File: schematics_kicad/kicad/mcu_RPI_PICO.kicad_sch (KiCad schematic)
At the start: 0 parts

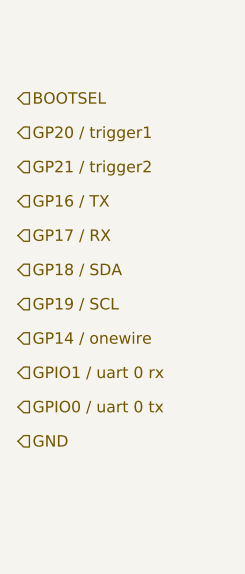
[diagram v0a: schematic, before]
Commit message: Updating schematics for RPI_PICO_W for tentacle v0.4
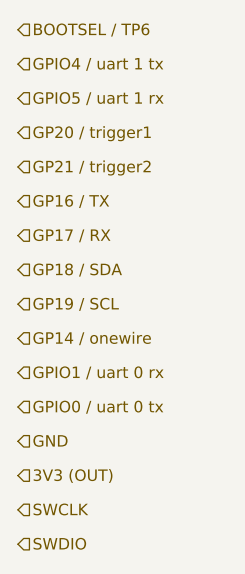
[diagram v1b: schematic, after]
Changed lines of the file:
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@@
 		(shape input)
 		(at 82.55 91.44 0)
-		(fields_autoplaced yes)
 		(effects
 			(font
@@
 		(shape input)
 		(at 82.55 99.06 0)
-		(fields_autoplaced yes)
 		(effects
 			(font
@@
 		(shape input)
 		(at 82.55 64.77 0)
-		(fields_autoplaced yes)
 		(effects
 			(font
@@
 		(shape input)
 		(at 82.55 83.82 0)
-		(fields_autoplaced yes)
 		(effects
 			(font
@@
 		(shape input)
 		(at 82.55 95.25 0)
-		(fields_autoplaced yes)
 		(effects
 			(font
@@
 		(shape input)
 		(at 82.55 87.63 0)
-		(fields_autoplaced yes)
+		(effects
+			(font
+				(size 1.27 1.27)
+			)
+			(justify left)
+		)
+	)
+	(hierarchical_label "GPIO4 {slash} uart 1 tx"
+		(shape input)
+		(at 82.55 57.15 0)
+		(effects
+			(font
+				(size 1.27 1.27)
+			)
+			(justify left)
+		)
+	)
+	(hierarchical_label "3V3 (OUT)"
+		(shape input)
+		(at 82.55 102.87 0)
+		(effects
+			(font
+				(size 1.27 1.27)
+			)
+			(justify left)
+		)
+	)
+	(hierarchical_label "SWDIO"
+		(shape input)
+		(at 82.55 110.49 0)
 		(effects
 			(font
@@
 		(shape input)
 		(at 82.55 80.01 0)
-		(fields_autoplaced yes)
 		(effects
 			(font
@@
 		(shape input)
 		(at 82.55 76.2 0)
-		(fields_autoplaced yes)
 		(effects
 			(font
@@
 		)
 	)
-	(hierarchical_label "BOOTSEL"
+	(hierarchical_label "SWCLK"
+		(shape input)
+		(at 82.55 106.68 0)
+		(effects
+			(font
+				(size 1.27 1.27)
+			)
+			(justify left)
+		)
+	)
+	(hierarchical_label "GPIO5 {slash} uart 1 rx"
 		(shape input)
 		(at 82.55 60.96 0)
-		(fields_autoplaced yes)
+		(effects
+			(font
+				(size 1.27 1.27)
+			)
+			(justify left)
+		)
+	)
+	(hierarchical_label "BOOTSEL {slash} TP6"
+		(shape input)
+		(at 82.55 53.34 0)
 		(effects
 			(font
@@
 		(shape input)
 		(at 82.55 68.58 0)
-		(fields_autoplaced yes)
 		(effects
 			(font
@@
 		(shape input)
 		(at 82.55 72.39 0)
-		(fields_autoplaced yes)
 		(effects
 			(font
